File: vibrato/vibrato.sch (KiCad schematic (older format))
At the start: 23 parts, among them J1 osc_out, J2 intensity pot (1M), J3 B+, J4 osc_in, J5 earth, J6 filament, J7 speed pot (250K), J8 footswitch

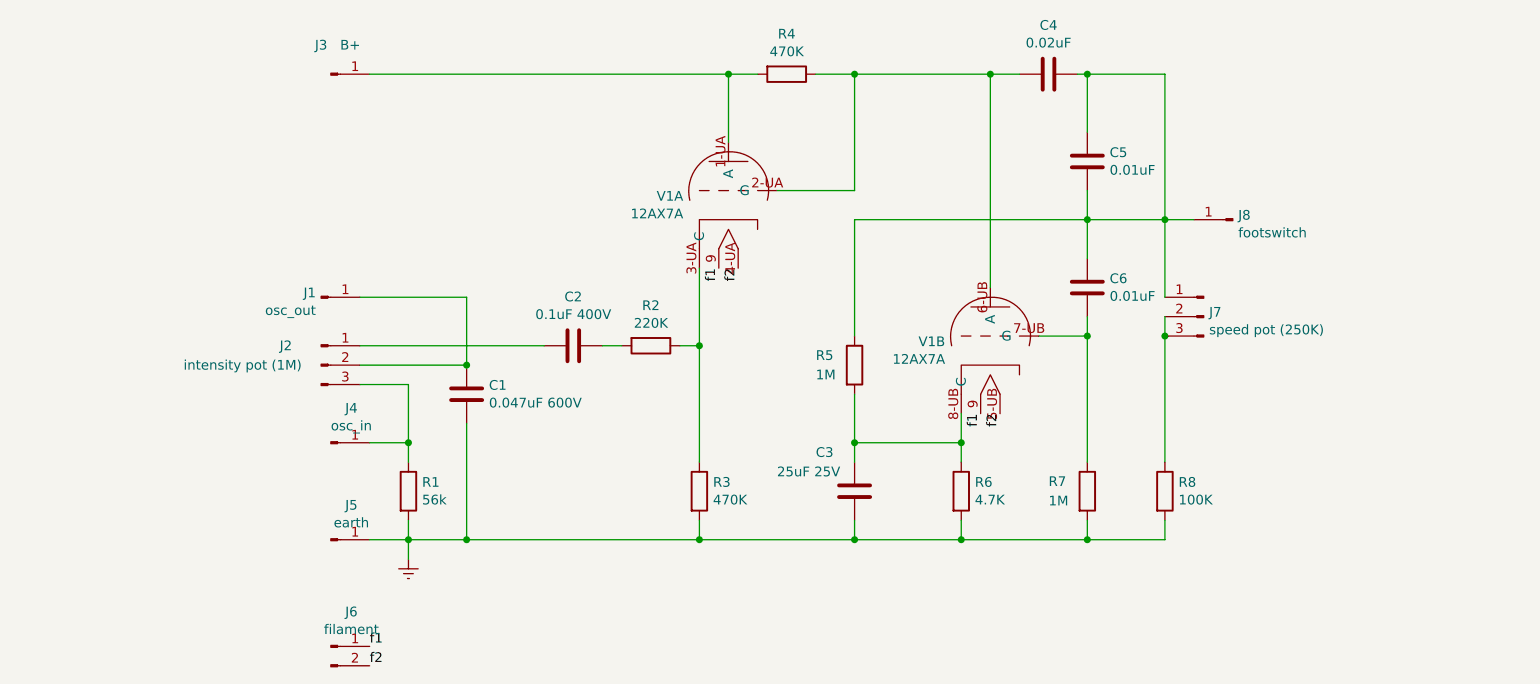
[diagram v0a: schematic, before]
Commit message: Refine schematics
Describe the parts that are mounted on the chassis
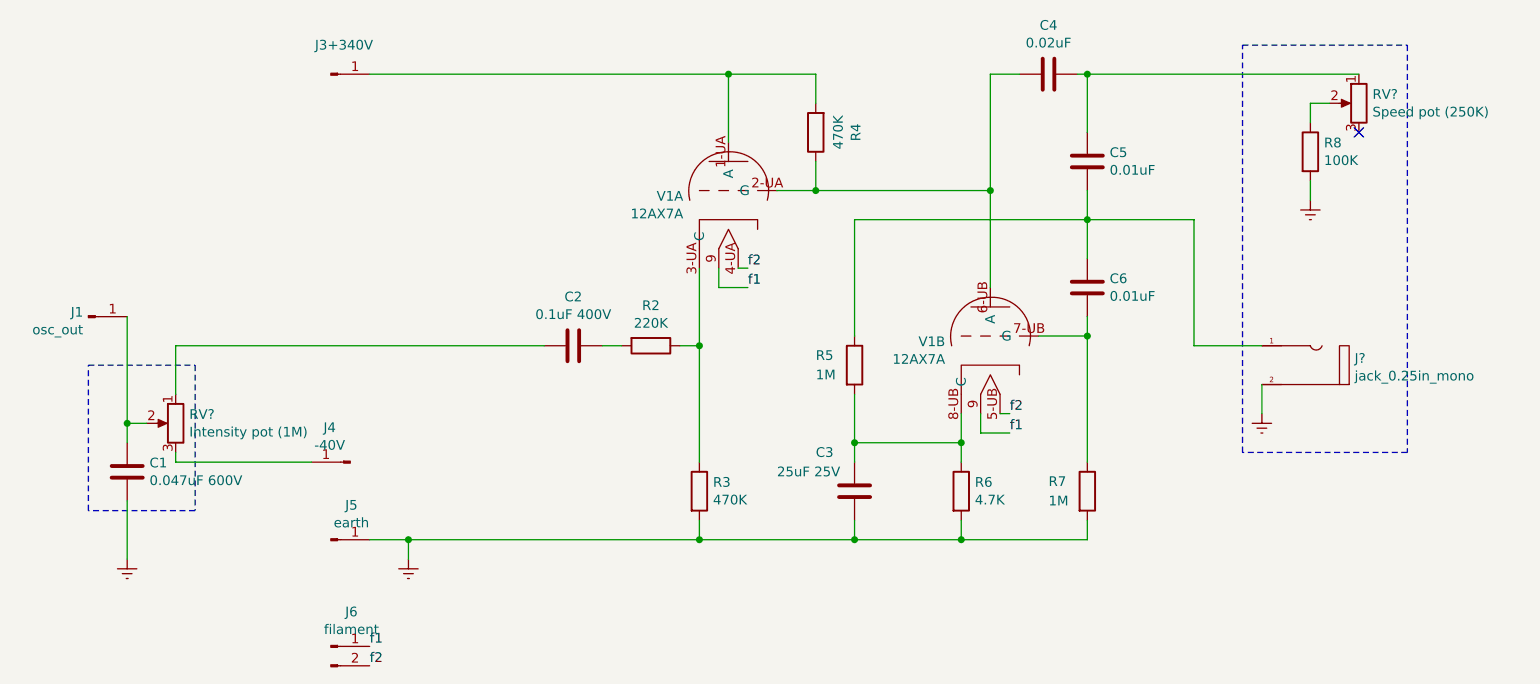
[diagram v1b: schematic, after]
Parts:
- removed J2: intensity pot (1M), symbol Connector:Conn_01x03_Male
- removed J7: speed pot (250K), symbol Connector:Conn_01x03_Male
- removed J8: footswitch, symbol Connector:Conn_01x01_Male
- removed R1: 56k, symbol Device:R
- added J?: jack_0.25in_mono, symbol yga1:jack_0.25in_mono
- added RV?: Speed pot (250K), symbol Device:R_POT
- added RV?: Intensity pot (1M), symbol Device:R_POT
- J3: value B+ -> +340V
- J4: value osc_in -> -40V
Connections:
- net Earth: now also J?.2
- net at J4.1 (Pin_1): now also RV?.3
- net at C2.2: now also RV?.1
- net at C1.1, J1.1 (Pin_1): now also RV?.2
- net at C5.2, C6.1, R5.1: now also J?.1; no longer C4.1, C5.1
- net at R8.1: now also RV?.2
- new net: C4.1, C5.1, RV?.1
- no-connect marks 0 -> 1
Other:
- moved on the sheet: C1, J1, J4, R4, R8
